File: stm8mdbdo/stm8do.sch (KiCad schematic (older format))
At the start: 6 parts, among them U1 STM8S003F3P

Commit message: Готова схема. Проверить все посадочные места, уточнить схему входов, выходов.
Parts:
- removed J?: Jack-DC, symbol Jack-DC
- added C1, C10, C11, C2, C8, C9: C_Small, Capacitors_SMD:C_0805_HandSoldering, symbol C_Small
- added C5: 0.1 uF, symbol C_Small
- added C6: 470 nF, symbol C_Small
- added C7: CP_Small, symbol CP_Small
- added D1: SS36, Diodes_SMD:DO-214AB_Handsoldering, symbol D
- added D10, D11, D8, D9: BTS4140N, TO_SOT_Packages_SMD:SOT-223, symbol BTS4140N
- added D2: D, Diodes_SMD:D_0805, symbol D
- added D3, D4, D5, D6, D7: LED, symbol LED
- added L1: INDUCTOR, Inductors:Inductor_Taiyo-Yuden_NR-80xx_HandSoldering, symbol INDUCTOR
- added P1, P4: CONN_01X02, symbol CONN_01X02
- added P2, P3: CONN_01X04, symbol CONN_01X04
- added P5: CONN_01X05, Connectors_Phoenix:PhoenixContact_MSTBV-GF_05x5.08mm_Vertical_ThreadedFlange, symbol CONN_01X05
- added R1: 0.33, symbol R
- added R10, R11, R12, R13: R, Resistors_SMD:R_0805_HandSoldering, symbol R
- added R3: 3.6k, Resistors_SMD:R_0805_HandSoldering, symbol R
- added R4, R5, R6: 1k, Resistors_SMD:R_0805_HandSoldering, symbol R
- added R7, R8, R9: 10K, Resistors_SMD:R_0805_HandSoldering, symbol R
- added RN1: R_Pack05, Resistors_SMD:R_Array_Convex_5x1206, symbol R_Pack05
- added U3: OPTO-TRANSISTOR-4, Opto-Devices:Optocoupler_SMD_ReflowWaveSoldering_KPC357_LTV35x_PC357_SingleChannel, symbol OPTO-TRANSISTOR-4
- added Y1: Crystal, symbol Crystal
- C4: renamed from C?; footprint (none) -> Capacitors_SMD:C_0805_HandSoldering
- R2: renamed from R?; value R -> 1.2k; footprint (none) -> Resistors_SMD:R_0805_HandSoldering
- gave numbers to parts that had none: 2
- renumbered U1 to U2
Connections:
- net labels added: AIN1, AIN2, DI, GND, IN/OUT, IN1, IN2, IN3, OUT1, OUT2, OUT3, OUT4, RO, STATUS, SWIM_RST, Vbb
- net labels removed: UART_RX, UART_TX, VSS
- wire segments 5 -> 137
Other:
- note added: "DC/DC"
- note added: "Аналоговые входа"
- note added: "Дискретные входы"
- note added: "Дискретные выходы"
- note added: "Индикация сотсояния выходов"
- note added: "Разъем для программирования"
- note added: "Фильтрация питания контроллера"
- moved on the sheet: C3, C4, R2, U1, U2

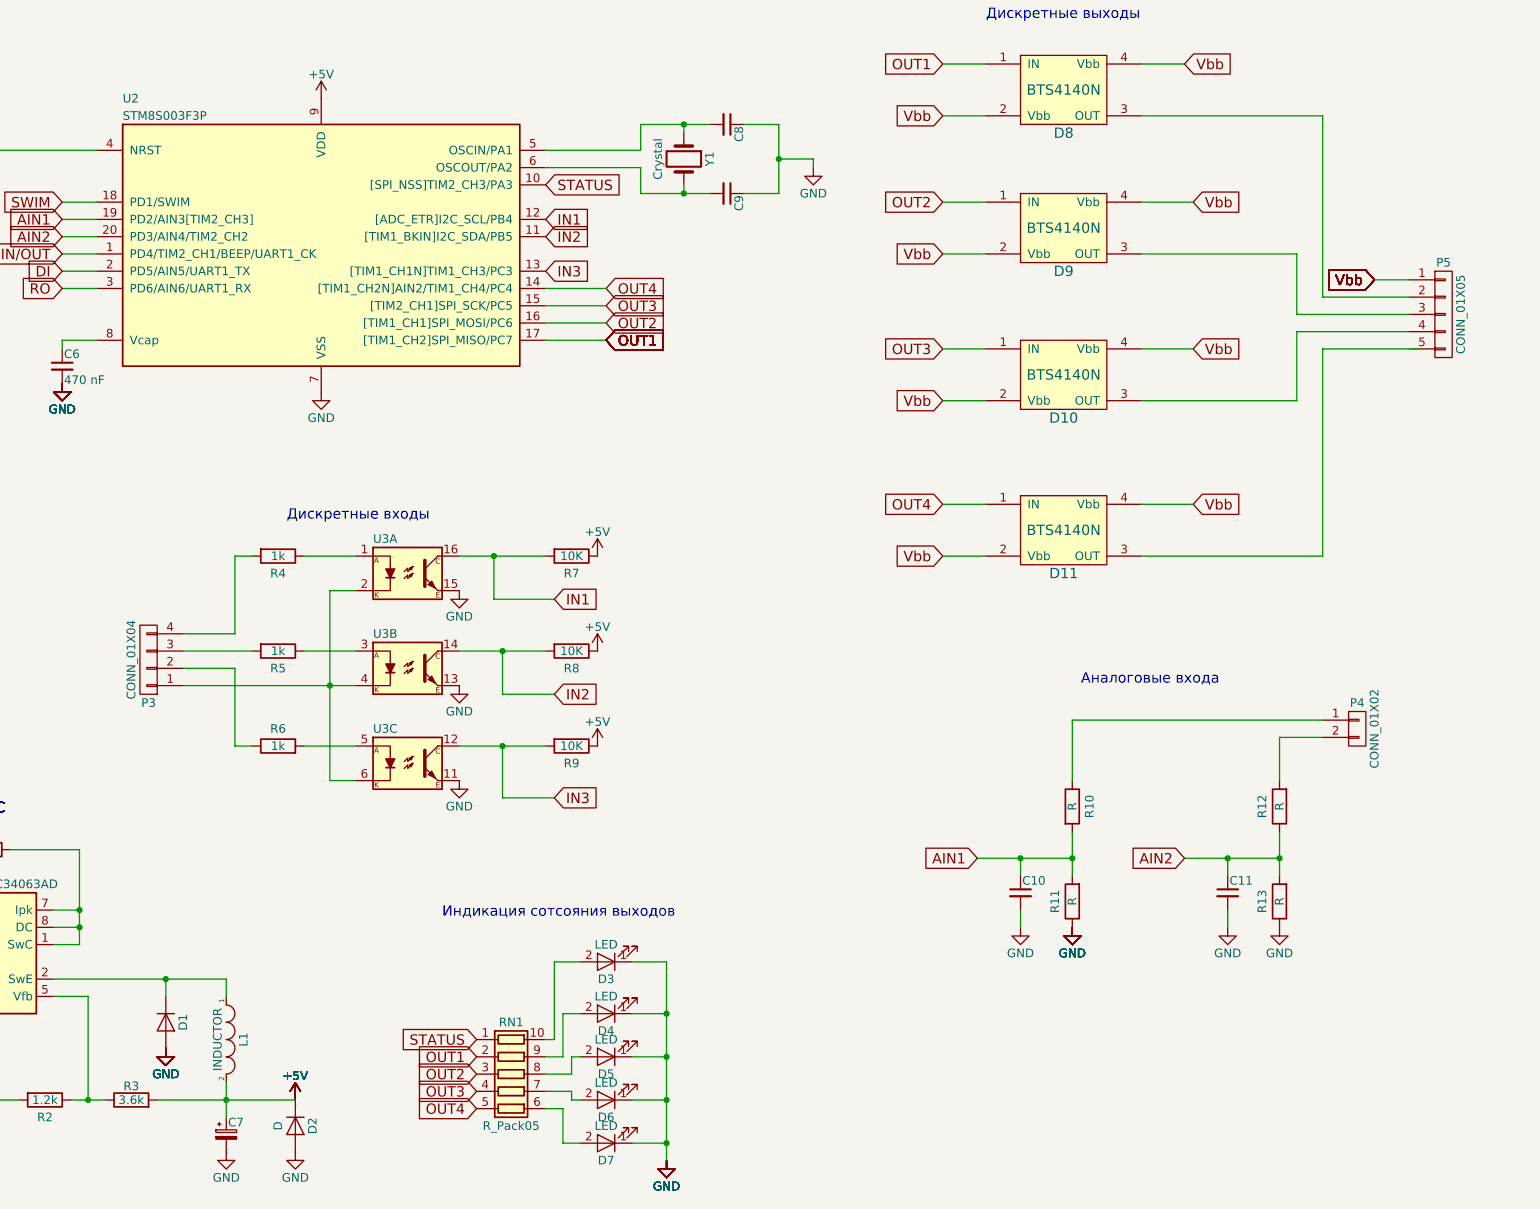
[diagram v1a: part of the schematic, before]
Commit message: Решена проблемма с библиотекой для конденсаторов. Просто сделал копию папки с именем которое содержится в ошибке.
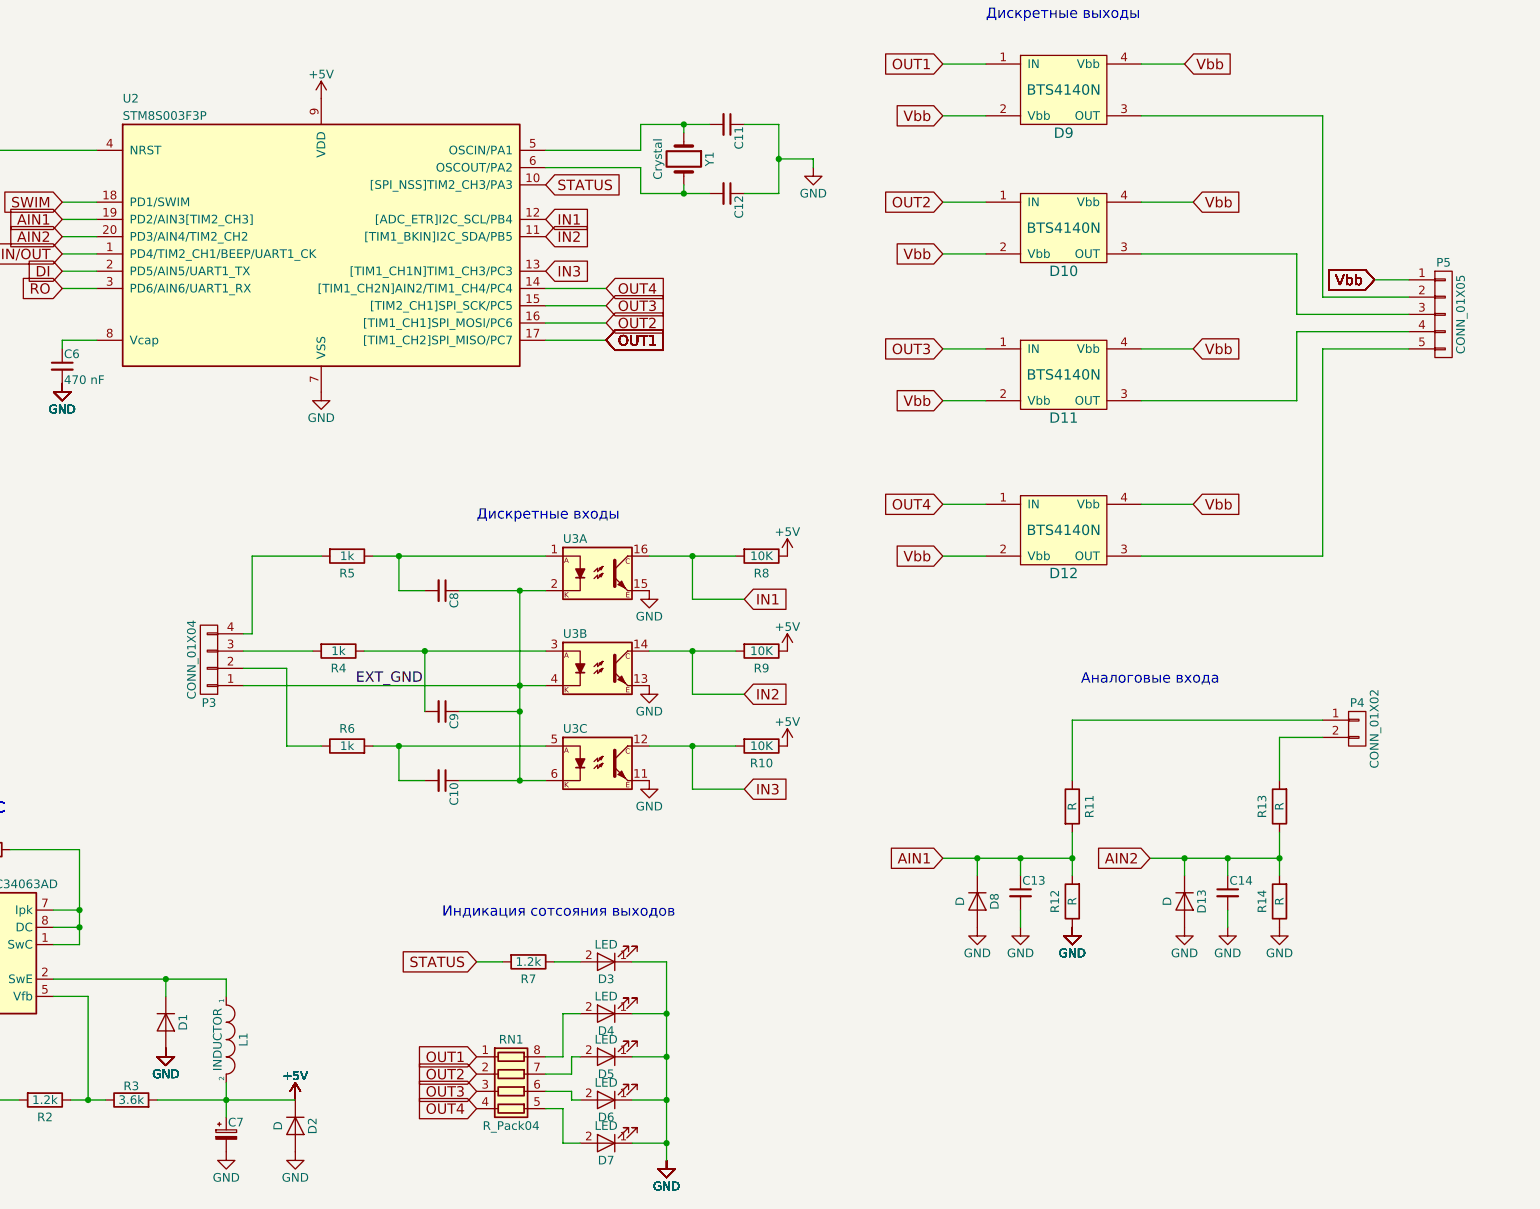
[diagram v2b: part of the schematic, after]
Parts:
- removed RN1: R_Pack05, Resistors_SMD:R_Array_Convex_5x1206, symbol R_Pack05
- added C10, C8, C9: C_Small, Capacitors_SMD:C_0805_HandSoldering, symbol C_Small
- added D13, D8: D, Diodes_SMD:D_0805, symbol D
- added R7: 1.2k, Resistors_SMD:R_0805_HandSoldering, symbol R
- added RN1: R_Pack04, symbol R_Pack04
- C3: value CP_Small -> 470uF; footprint (none) -> Capacitors_THT:C_Radial_D10_L16_P5
- C7: footprint (none) -> Capacitors_THT:C_Radial_D10_L16_P5
- renumbered C8 to C11, C9 to C12, C10 to C13, C11 to C14, D9 to D10, D10 to D11, D11 to D12, D8 to D9, R9 to R10, R10 to R11, R11 to R12, R12 to R13, R13 to R14, R5 to R4, R4 to R5, R7 to R8, R8 to R9
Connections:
- net AIN1: now also D8.1 (K)
- net AIN2: now also D13.1 (K)
- net GND: now also D13.2 (A), D8.2 (A)
- net OUT1: now also RN1.1 (R1.1)
- net OUT2: now also RN1.2 (R2.1)
- net OUT3: now also RN1.3 (R3.1)
- net OUT4: now also RN1.4 (R4.1)
- net STATUS: now also R7.2
- net at D12.3 (OUT): now also P5.5 (P5)
- net at D4.2 (A): now also RN1.8 (R1.2)
- net at D5.2 (A): now also RN1.7 (R2.2)
- net at D6.2 (A): now also RN1.6 (R3.2)
- net at D3.2 (A): now also R7.1
- net at D7.2 (A): now also RN1.5 (R4.2)
- net at R5.1, U3.1: now also C8.2
- net EXT_GND: now reaches P3.1 (P1), U3.2, U3.4, U3.6
- net EXT_GND: now also C10.1, C8.1, C9.1
- net at R4.1, U3.3: now also C9.2
- net at R6.2, U3.5: now also C10.2
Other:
- moved on the sheet: P3, R10, R4, R5, R6, R8, R9, U3A, U3B, U3C

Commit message: Перевод на новую библиотеку со спасением старых
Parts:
- removed U3: OPTO-TRANSISTOR-4, Opto-Devices:Optocoupler_SMD_ReflowWaveSoldering_KPC357_LTV35x_PC357_SingleChannel, symbol OPTO-TRANSISTOR-4
- added U3, U4, U5: TLP185, Package_SO:SOIC-4_4.55x3.7mm_P2.54mm, symbol Isolator:TLP185
- C1, C11, C12, C13, C14, C2, C4, C5, C6: symbol C_Small -> Device:C_Small
- C10, C8, C9: value C_Small -> 470pF; symbol C_Small -> Device:C_Small
- C3, C7: footprint Capacitors_THT:C_Radial_D10_L16_P5 -> Capacitor_THT:CP_Radial_D10.0mm_P5.00mm; symbol CP_Small -> Device:CP_Small
- D1, D13, D2, D8: symbol D -> Device:D
- D10, D11, D12, D9: symbol BTS4140N -> stm8do-rescue:BTS4140N
- D3, D4, D5, D6, D7: symbol LED -> Device:LED
- L1: symbol INDUCTOR -> stm8do-rescue:INDUCTOR
- P1, P4: symbol CONN_01X02 -> stm8do-rescue:CONN_01X02
- P2, P3: symbol CONN_01X04 -> stm8do-rescue:CONN_01X04
- P5: symbol CONN_01X05 -> stm8do-rescue:CONN_01X05
- R1, R10, R11, R12, R13, R14, R2, R3, R4, R5, R6, R7, R8, R9: symbol R -> Device:R
- RN1: symbol R_Pack04 -> Device:R_Pack04
- U1: symbol MC34063AD -> stm8do-rescue:MC34063AD
- U2: symbol STM8S003F3P -> stm8do-rescue:STM8S003F3P
- Y1: symbol Crystal -> Device:Crystal
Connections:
- net EXT_GND: now also U3.3, U4.3, U5.3
- net GND: now also U3.4, U4.4, U5.4
- net IN1: now also U3.6
- net IN2: now also U4.6
- net IN3: now also U5.6
- net at C8.2, R5.1: now also U3.1
- net at C9.2, R4.1: now also U4.1
- net at C10.2, R6.2: now also U5.1

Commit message: Auto
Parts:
- D3, D4, D5, D6, D7: footprint (none) -> LED_SMD:LED_0805_2012Metric_Pad1.15x1.40mm_HandSolder
- R1: footprint (none) -> Resistor_SMD:R_0805_2012Metric_Pad1.15x1.40mm_HandSolder
- Y1: footprint (none) -> Crystal:Crystal_SMD_HC49-SD_HandSoldering
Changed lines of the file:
@@
 F 0 "R1" V 2480 5450 50  0000 C CNN
 F 1 "0.33" V 2400 5450 50  0000 C CNN
-F 2 "" V 2330 5450 50  0000 C CNN
+F 2 "Resistor_SMD:R_0805_2012Metric_Pad1.15x1.40mm_HandSolder" V 2330 5450 50  0001 C CNN
 F 3 "" H 2400 5450 50  0000 C CNN
 	1    2400 5450
@@
 F 0 "D4" H 6000 6500 50  0000 C CNN
 F 1 "LED" H 6000 6300 50  0000 C CNN
-F 2 "" H 6000 6400 50  0000 C CNN
+F 2 "LED_SMD:LED_0805_2012Metric_Pad1.15x1.40mm_HandSolder" H 6000 6400 50  0001 C CNN
 F 3 "" H 6000 6400 50  0000 C CNN
 	1    6000 6400
@@
 F 0 "D5" H 6000 6750 50  0000 C CNN
 F 1 "LED" H 6000 6550 50  0000 C CNN
-F 2 "" H 6000 6650 50  0000 C CNN
+F 2 "LED_SMD:LED_0805_2012Metric_Pad1.15x1.40mm_HandSolder" H 6000 6650 50  0001 C CNN
 F 3 "" H 6000 6650 50  0000 C CNN
 	1    6000 6650
@@
 F 0 "D6" H 6000 7000 50  0000 C CNN
 F 1 "LED" H 6000 6800 50  0000 C CNN
-F 2 "" H 6000 6900 50  0000 C CNN
+F 2 "LED_SMD:LED_0805_2012Metric_Pad1.15x1.40mm_HandSolder" H 6000 6900 50  0001 C CNN
 F 3 "" H 6000 6900 50  0000 C CNN
 	1    6000 6900
@@
 F 0 "D3" H 6000 6200 50  0000 C CNN
 F 1 "LED" H 6000 6000 50  0000 C CNN
-F 2 "" H 6000 6100 50  0000 C CNN
+F 2 "LED_SMD:LED_0805_2012Metric_Pad1.15x1.40mm_HandSolder" H 6000 6100 50  0001 C CNN
 F 3 "" H 6000 6100 50  0000 C CNN
 	1    6000 6100
@@
 F 0 "D7" H 6000 7250 50  0000 C CNN
 F 1 "LED" H 6000 7050 50  0000 C CNN
-F 2 "" H 6000 7150 50  0000 C CNN
+F 2 "LED_SMD:LED_0805_2012Metric_Pad1.15x1.40mm_HandSolder" H 6000 7150 50  0001 C CNN
 F 3 "" H 6000 7150 50  0000 C CNN
 	1    6000 7150
@@
 F 0 "Y1" H 6450 1600 50  0000 C CNN
 F 1 "Crystal" H 6450 1300 50  0000 C CNN
-F 2 "" H 6450 1450 50  0000 C CNN
+F 2 "Crystal:Crystal_SMD_HC49-SD_HandSoldering" H 6450 1450 50  0001 C CNN
 F 3 "" H 6450 1450 50  0000 C CNN
 	1    6450 1450

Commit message: Auto commit date
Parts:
- C5, C6: footprint (none) -> Capacitor_SMD:C_0805_2012Metric_Pad1.15x1.40mm_HandSolder
- RN1: footprint (none) -> Resistor_THT:R_Array_SIP4
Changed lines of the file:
@@
 F 0 "C6" H 2860 2720 50  0000 L CNN
 F 1 "470 nF" H 2860 2570 50  0000 L CNN
-F 2 "" H 2850 2650 50  0000 C CNN
+F 2 "Capacitor_SMD:C_0805_2012Metric_Pad1.15x1.40mm_HandSolder" H 2850 2650 50  0001 C CNN
 F 3 "" H 2850 2650 50  0000 C CNN
 	1    2850 2650
@@
 F 0 "P4" H 10350 4900 50  0000 C CNN
 F 1 "CONN_01X02" V 10450 4750 50  0000 C CNN
-F 2 "" H 10350 4750 50  0000 C CNN
+F 2 "" H 10350 4750 50  0001 C CNN
 F 3 "" H 10350 4750 50  0000 C CNN
 	1    10350 4750
@@
 F 0 "C5" H 2210 1670 50  0000 L CNN
 F 1 "0.1 uF" H 2210 1520 50  0000 L CNN
-F 2 "" H 2200 1600 50  0000 C CNN
+F 2 "Capacitor_SMD:C_0805_2012Metric_Pad1.15x1.40mm_HandSolder" H 2200 1600 50  0001 C CNN
 F 3 "" H 2200 1600 50  0000 C CNN
 	1    2200 1600
@@
 F 0 "P1" H 900 6000 50  0000 C CNN
 F 1 "CONN_01X02" V 1000 5850 50  0000 C CNN
-F 2 "" H 900 5850 50  0000 C CNN
+F 2 "" H 900 5850 50  0001 C CNN
 F 3 "" H 900 5850 50  0000 C CNN
 	1    900  5850
@@
 F 0 "P2" H 1150 3700 50  0000 C CNN
 F 1 "CONN_01X04" V 1250 3450 50  0000 C CNN
-F 2 "" H 1150 3450 50  0000 C CNN
+F 2 "" H 1150 3450 50  0001 C CNN
 F 3 "" H 1150 3450 50  0000 C CNN
 	1    1150 3450
@@
 F 0 "P3" H 3700 4600 50  0000 C CNN
 F 1 "CONN_01X04" V 3800 4350 50  0000 C CNN
-F 2 "" H 3700 4350 50  0000 C CNN
+F 2 "" H 3700 4350 50  0001 C CNN
 F 3 "" H 3700 4350 50  0000 C CNN
 	1    3700 4350
@@
 F 0 "RN1" V 5150 6850 50  0000 C CNN
 F 1 "R_Pack04" V 5650 6850 50  0000 C CNN
-F 2 "" V 5725 6850 50  0001 C CNN
+F 2 "Resistor_THT:R_Array_SIP4" V 5725 6850 50  0001 C CNN
 F 3 "" H 5450 6850 50  0000 C CNN
 	1    5450 6850

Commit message: Auto commit
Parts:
- C1, C10, C13, C14, C2, C4, C8, C9: footprint Capacitors_SMD:C_0805_HandSoldering -> Capacitor_SMD:C_0805_2012Metric_Pad1.15x1.40mm_HandSolder
- C11, C12: value C_Small -> 22pF; footprint Capacitors_SMD:C_0805_HandSoldering -> Capacitor_SMD:C_0805_2012Metric_Pad1.15x1.40mm_HandSolder
- D1: footprint Diodes_SMD:DO-214AB_Handsoldering -> Diode_SMD:D_SMC
- D10, D11, D12, D9: footprint TO_SOT_Packages_SMD:SOT-223 -> Package_TO_SOT_SMD:SOT-223
- D13, D8: value D -> MM3Z5V1; footprint Diodes_SMD:D_0805 -> Diode_SMD:D_0805_2012Metric
- D2: value D -> MM3Z5V1; footprint Diodes_SMD:D_0805 -> Diode_SMD:D_0805_2012Metric_Pad1.15x1.40mm_HandSolder
- L1: value INDUCTOR -> 220uH; footprint Inductors:Inductor_Taiyo-Yuden_NR-80xx_HandSoldering -> Inductor_SMD:L_2816_7142Metric_Pad3.20x4.45mm_HandSolder
- P1, P4: footprint (none) -> Connector_PinHeader_1.27mm:PinHeader_1x02_P1.27mm_Vertical_SMD_Pin1Left
- P2, P3: footprint (none) -> Connector_PinHeader_1.27mm:PinHeader_1x04_P1.27mm_Horizontal
- P5: footprint Connectors_Phoenix:PhoenixContact_MSTBV-GF_05x5.08mm_Vertical_ThreadedFlange -> Connector_PinHeader_1.27mm:PinHeader_1x05_P1.27mm_Vertical_SMD_Pin1Left
- R10, R11, R12, R13, R14, R2, R3, R4, R5, R6, R7, R8, R9: footprint Resistors_SMD:R_0805_HandSoldering -> Resistor_SMD:R_0805_2012Metric_Pad1.15x1.40mm_HandSolder
- RN1: footprint Resistor_THT:R_Array_SIP4 -> Resistor_SMD:R_Array_Concave_4x0603
- U1: footprint Housings_SOIC:SOIC-8_3.9x4.9mm_Pitch1.27mm -> Package_SO:SOIC-8_3.9x4.9mm_P1.27mm
- U2: footprint Housings_SSOP:TSSOP-20_4.4x6.5mm_Pitch0.65mm -> Package_SO:TSSOP-20_4.4x6.5mm_P0.65mm
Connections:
- net OUT1: now also RN1.5 (R4.2); no longer RN1.1 (R1.1)
- net OUT2: now also RN1.6 (R3.2); no longer RN1.2 (R2.1)
- net OUT3: now also RN1.7 (R2.2); no longer RN1.3 (R3.1)
- net OUT4: now also RN1.8 (R1.2); no longer RN1.4 (R4.1)
- net at D4.2 (A): now also RN1.4 (R4.1); no longer RN1.8 (R1.2)
- net at D5.2 (A): now also RN1.3 (R3.1); no longer RN1.7 (R2.2)
- net at D6.2 (A): now also RN1.2 (R2.1); no longer RN1.6 (R3.2)
- net at D7.2 (A): now also RN1.1 (R1.1); no longer RN1.5 (R4.2)

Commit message: Auto commit
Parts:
- C4: value C_Small -> 470pF
- C7: value CP_Small -> 100uF
- P2: value CONN_01X04 -> PRG; footprint Connector_PinHeader_1.27mm:PinHeader_1x04_P1.27mm_Horizontal -> Connector_PinHeader_1.27mm:PinHeader_1x04_P1.27mm_Vertical
- P3: value CONN_01X04 -> DIN
- P4: value CONN_01X02 -> AIN
- P5: value CONN_01X05 -> DO
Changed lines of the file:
@@
 P 1800 6300
 F 0 "C4" H 1810 6370 50  0000 L CNN
-F 1 "C_Small" H 1810 6220 50  0001 L CNN
+F 1 "470pF" H 1810 6220 50  0001 L CNN
 F 2 "Capacitor_SMD:C_0805_2012Metric_Pad1.15x1.40mm_HandSolder" H 1800 6300 50  0001 C CNN
 F 3 "" H 1800 6300 50  0000 C CNN
@@
 P 3800 7100
 F 0 "C7" H 3810 7170 50  0000 L CNN
-F 1 "CP_Small" H 3810 7020 50  0001 L CNN
+F 1 "100uF" H 3810 7020 50  0001 L CNN
 F 2 "Capacitor_THT:CP_Radial_D10.0mm_P5.00mm" H 3800 7100 50  0001 C CNN
 F 3 "" H 3800 7100 50  0000 C CNN
@@
 P 10850 2350
 F 0 "P5" H 10850 2650 50  0000 C CNN
-F 1 "CONN_01X05" V 10950 2350 50  0000 C CNN
+F 1 "DO" V 10950 2350 50  0000 C CNN
 F 2 "Connector_PinHeader_1.27mm:PinHeader_1x05_P1.27mm_Vertical_SMD_Pin1Left" H 10850 2350 50  0001 C CNN
 F 3 "" H 10850 2350 50  0000 C CNN
@@
 P 10350 4750
 F 0 "P4" H 10350 4900 50  0000 C CNN
-F 1 "CONN_01X02" V 10450 4750 50  0000 C CNN
+F 1 "AIN" V 10450 4750 50  0000 C CNN
 F 2 "Connector_PinHeader_1.27mm:PinHeader_1x02_P1.27mm_Vertical_SMD_Pin1Left" H 10350 4750 50  0001 C CNN
 F 3 "" H 10350 4750 50  0000 C CNN
@@
 P 1150 3450
 F 0 "P2" H 1150 3700 50  0000 C CNN
-F 1 "CONN_01X04" V 1250 3450 50  0000 C CNN
-F 2 "Connector_PinHeader_1.27mm:PinHeader_1x04_P1.27mm_Horizontal" H 1150 3450 50  0001 C CNN
+F 1 "PRG" V 1250 3450 50  0000 C CNN
+F 2 "Connector_PinHeader_1.27mm:PinHeader_1x04_P1.27mm_Vertical" H 1150 3450 50  0001 C CNN
 F 3 "" H 1150 3450 50  0000 C CNN
 	1    1150 3450
@@
 P 3700 4350
 F 0 "P3" H 3700 4600 50  0000 C CNN
-F 1 "CONN_01X04" V 3800 4350 50  0000 C CNN
+F 1 "DIN" V 3800 4350 50  0000 C CNN
 F 2 "Connector_PinHeader_1.27mm:PinHeader_1x04_P1.27mm_Horizontal" H 3700 4350 50  0001 C CNN
 F 3 "" H 3700 4350 50  0000 C CNN

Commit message: Auto commit
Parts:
- P5: footprint Connector_PinHeader_1.27mm:PinHeader_1x05_P1.27mm_Vertical_SMD_Pin1Left -> Connector_PinHeader_1.27mm:PinHeader_1x05_P1.27mm_Vertical
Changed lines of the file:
@@
 F 0 "P5" H 10850 2650 50  0000 C CNN
 F 1 "DO" V 10950 2350 50  0000 C CNN
-F 2 "Connector_PinHeader_1.27mm:PinHeader_1x05_P1.27mm_Vertical_SMD_Pin1Left" H 10850 2350 50  0001 C CNN
+F 2 "Connector_PinHeader_1.27mm:PinHeader_1x05_P1.27mm_Vertical" H 10850 2350 50  0001 C CNN
 F 3 "" H 10850 2350 50  0000 C CNN
 	1    10850 2350
